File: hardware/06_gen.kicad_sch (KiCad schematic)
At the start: 0 parts

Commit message: Generator sheet: R-2R ladder and output stage
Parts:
- added C19: 470pF C0G, symbol Device:C
- added C20: 1nF C0G, symbol Device:C
- added C21: 100nF, symbol Device:C
- added J11: BNC_GEN, symbol Connector:Conn_Coaxial
- added J12: LINK2, Package_LCC:PLCC-44_16.6x16.6mm_P1.27mm, symbol Connector_Generic:Conn_01x02
- added R22, R23, R25, R27, R29, R31, R33, R35, R37: 20k, symbol Device:R
- added R24, R26, R28, R30, R32, R34, R36, R38: 10k, symbol Device:R
- added R39: 51R, symbol Device:R
- added U10: MCP6292, Package_TO_SOT_SMD:SOT-353_SC-70-5, symbol Amplifier_Operational:Opamp_Dual
- added U9: ESP32-S3-N16R8-DEVBOARD, RF_Module:ESP32-C3-WROOM-02, symbol oscil:ESP32-S3-N16R8-DEVBOARD
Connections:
- new net: R32.1, R33.2, R34.2
- new net: R30.1, R31.2, R32.2
- new net: R22.1, R23.2, R24.2
- new net: R26.1, R27.2, R28.2
- new net: C20.2, R39.1, U10.1, U10.2 (-)
- new net: J11.1 (In), R39.2
- new net: R24.1, R25.2, R26.2
- new net: C20.1, R36.1, R37.2, R38.2
- new net: R34.1, R35.2, R36.2
- new net: R28.1, R29.2, R30.2
- new net: C19.1, R38.1, U10.3 (+)
- new net: U10.6 (-), U10.7
- new net +3V3_GEN: C21.1, U10.8 (V+), U9.1 (3V3)
- new net +5V: U9.21 (5V)
- new net DAC_D0: R23.1, U9.4 (IO4)
- new net DAC_D1: R25.1, U9.5 (IO5)
- new net DAC_D2: R27.1, U9.6 (IO6)
- new net DAC_D3: R29.1, U9.7 (IO7)
- new net DAC_D4: R31.1, U9.12 (IO8)
- new net DAC_D5: R33.1, U9.15 (IO9)
- new net DAC_D6: R35.1, U9.16 (IO10)
- new net DAC_D7: R37.1, U9.17 (IO11)
- new net GND: C19.2, C21.2, J11.2 (Ext), J12.2 (Pin_2), R22.2, U10.4 (V-), U10.5 (+), U9.22 (GND), U9.23 (GND), U9.24 (GND), U9.44 (GND)
- new net LINK2_RX: J12.1 (Pin_1), U9.42 (IO44_RX)
- no-connect marks 0 -> 29
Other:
- note added: "2-pole Sallen-Key, unity gain. Ladder output is 10k, R38 10k. fc ~23kHz, Q ~0.73. C0G required."
- note added: "IO48: onboard WS2812 status LED, driven over RMT."
- note added: "Output 0 to 3.3V unipolar, no gain/offset stage in Rev A. 51R isolates the op-amp from cable capacitance."

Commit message: Add final Rev A schematic PDF and edited footprints
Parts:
- C19, C20, C21: footprint (none) -> Capacitor_THT:C_Disc_D5.0mm_W2.5mm_P5.00mm
- J11: footprint (none) -> Connector_Coaxial:BNC_PanelMountable_Vertical
- J12: footprint Package_LCC:PLCC-44_16.6x16.6mm_P1.27mm -> Connector_PinHeader_2.54mm:PinHeader_1x02_P2.54mm_Vertical
- R22, R23, R24, R25, R26, R27, R28, R29, R30, R31, R32, R33, R34, R35, R36, R37, R38, R39: footprint (none) -> Resistor_THT:R_Axial_DIN0207_L6.3mm_D2.5mm_P10.16mm_Horizontal
- U10: footprint Package_TO_SOT_SMD:SOT-353_SC-70-5 -> Package_DIP:DIP-8_W7.62mm
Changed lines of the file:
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@@
 	(title_block
 		(title "Oscil")
-		(date "2026-09-18")
-		(rev "0.1")
+		(date "2026-09-21")
+		(rev "A")
 		(comment 1 "Two-channel Digital Oscilloscope and Function Generator")
 		(comment 2 "ESP32-S3 / ESP-IDF / FreeRTOS")
@@
 			)
 		)
-		(property "Footprint" ""
+		(property "Footprint" "Resistor_THT:R_Axial_DIN0207_L6.3mm_D2.5mm_P10.16mm_Horizontal"
 			(at 121.92 135.382 90)
 			(hide yes)
@@
 			)
 		)
-		(property "Footprint" ""
+		(property "Footprint" "Resistor_THT:R_Axial_DIN0207_L6.3mm_D2.5mm_P10.16mm_Horizontal"
 			(at 109.982 129.54 90)
 			(hide yes)
@@
 			)
 		)
-		(property "Footprint" ""
+		(property "Footprint" "Resistor_THT:R_Axial_DIN0207_L6.3mm_D2.5mm_P10.16mm_Horizontal"
 			(at 28.702 129.54 90)
 			(hide yes)
@@
 			)
 		)
-		(property "Footprint" "Package_LCC:PLCC-44_16.6x16.6mm_P1.27mm"
+		(property "Footprint" "Connector_PinHeader_2.54mm:PinHeader_1x02_P2.54mm_Vertical"
 			(at 166.37 90.17 0)
 			(hide yes)
@@
 			)
 		)
-		(property "Footprint" ""
+		(property "Footprint" "Resistor_THT:R_Axial_DIN0207_L6.3mm_D2.5mm_P10.16mm_Horizontal"
 			(at 69.342 129.54 90)
 			(hide yes)
@@
 			)
 		)
-		(property "Footprint" ""
+		(property "Footprint" "Resistor_THT:R_Axial_DIN0207_L6.3mm_D2.5mm_P10.16mm_Horizontal"
 			(at 236.22 141.478 90)
 			(hide yes)
@@
 			)
 		)
-		(property "Footprint" ""
+		(property "Footprint" "Resistor_THT:R_Axial_DIN0207_L6.3mm_D2.5mm_P10.16mm_Horizontal"
 			(at 40.64 135.382 90)
 			(hide yes)
@@
 			)
 		)
-		(property "Footprint" "Package_TO_SOT_SMD:SOT-353_SC-70-5"
+		(property "Footprint" "Package_DIP:DIP-8_W7.62mm"
 			(at 228.6 95.25 0)
 			(hide yes)
@@
 			)
 		)
-		(property "Footprint" ""
+		(property "Footprint" "Capacitor_THT:C_Disc_D5.0mm_W2.5mm_P5.00mm"
 			(at 239.7252 97.79 0)
 			(hide yes)
@@
 			)
 		)
-		(property "Footprint" ""
+		(property "Footprint" "Connector_Coaxial:BNC_PanelMountable_Vertical"
 			(at 247.65 139.7 0)
 			(hide yes)
@@
 			)
 		)
-		(property "Footprint" ""
+		(property "Footprint" "Resistor_THT:R_Axial_DIN0207_L6.3mm_D2.5mm_P10.16mm_Horizontal"
 			(at 162.56 135.382 90)
 			(hide yes)
@@
 			)
 		)
-		(property "Footprint" ""
+		(property "Footprint" "Resistor_THT:R_Axial_DIN0207_L6.3mm_D2.5mm_P10.16mm_Horizontal"
 			(at 49.022 129.54 90)
 			(hide yes)
@@
 			)
 		)
-		(property "Footprint" ""
+		(property "Footprint" "Resistor_THT:R_Axial_DIN0207_L6.3mm_D2.5mm_P10.16mm_Horizontal"
 			(at 89.662 129.54 90)
 			(hide yes)
@@
 			)
 		)
-		(property "Footprint" ""
+		(property "Footprint" "Resistor_THT:R_Axial_DIN0207_L6.3mm_D2.5mm_P10.16mm_Horizontal"
 			(at 170.942 129.54 90)
 			(hide yes)
@@
 			)
 		)
-		(property "Footprint" ""
+		(property "Footprint" "Capacitor_THT:C_Disc_D5.0mm_W2.5mm_P5.00mm"
 			(at 191.77 123.4948 0)
 			(hide yes)
@@
 			)
 		)
-		(property "Footprint" ""
+		(property "Footprint" "Resistor_THT:R_Axial_DIN0207_L6.3mm_D2.5mm_P10.16mm_Horizontal"
 			(at 130.302 129.54 90)
 			(hide yes)
@@
 			)
 		)
-		(property "Footprint" ""
+		(property "Footprint" "Resistor_THT:R_Axial_DIN0207_L6.3mm_D2.5mm_P10.16mm_Horizontal"
 			(at 28.702 143.51 90)
 			(hide yes)
@@
 			)
 		)
-		(property "Footprint" ""
+		(property "Footprint" "Resistor_THT:R_Axial_DIN0207_L6.3mm_D2.5mm_P10.16mm_Horizontal"
 			(at 101.6 135.382 90)
 			(hide yes)
@@
 			)
 		)
-		(property "Footprint" ""
+		(property "Footprint" "Capacitor_THT:C_Disc_D5.0mm_W2.5mm_P5.00mm"
 			(at 196.5452 146.05 0)
 			(hide yes)
@@
 			)
 		)
-		(property "Footprint" ""
+		(property "Footprint" "Resistor_THT:R_Axial_DIN0207_L6.3mm_D2.5mm_P10.16mm_Horizontal"
 			(at 60.96 135.382 90)
 			(hide yes)
@@
 			)
 		)
-		(property "Footprint" "Package_TO_SOT_SMD:SOT-353_SC-70-5"
+		(property "Footprint" "Package_DIP:DIP-8_W7.62mm"
 			(at 220.98 139.7 0)
 			(hide yes)
@@
 			)
 		)
-		(property "Footprint" ""
+		(property "Footprint" "Resistor_THT:R_Axial_DIN0207_L6.3mm_D2.5mm_P10.16mm_Horizontal"
 			(at 142.24 135.382 90)
 			(hide yes)
@@
 			)
 		)
-		(property "Footprint" ""
+		(property "Footprint" "Resistor_THT:R_Axial_DIN0207_L6.3mm_D2.5mm_P10.16mm_Horizontal"
 			(at 81.28 135.382 90)
 			(hide yes)
@@
 			)
 		)
-		(property "Footprint" "Package_TO_SOT_SMD:SOT-353_SC-70-5"
+		(property "Footprint" "Package_DIP:DIP-8_W7.62mm"
 			(at 195.58 92.71 0)
 			(hide yes)
@@
 			)
 		)
-		(property "Footprint" ""
+		(property "Footprint" "Resistor_THT:R_Axial_DIN0207_L6.3mm_D2.5mm_P10.16mm_Horizontal"
 			(at 150.622 129.54 90)
 			(hide yes)
@@
 			)
 		)
-		(property "Footprint" ""
+		(property "Footprint" "Resistor_THT:R_Axial_DIN0207_L6.3mm_D2.5mm_P10.16mm_Horizontal"
 			(at 187.96 135.382 90)
 			(hide yes)

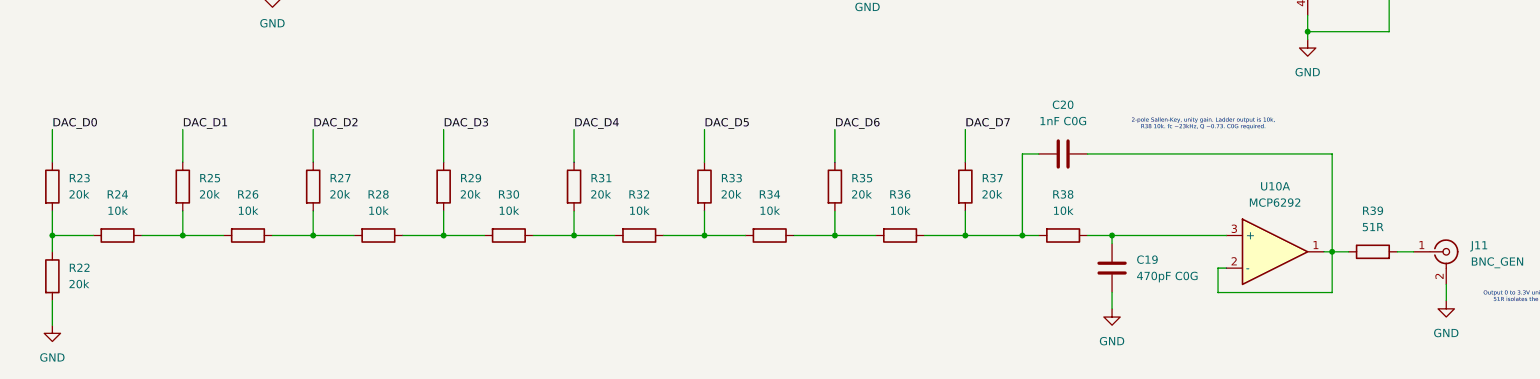
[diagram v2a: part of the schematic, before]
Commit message: hardware: generator ladder all 10k, R as parallel pairs, filter corner now 33 kHz; schematic exports regenerated
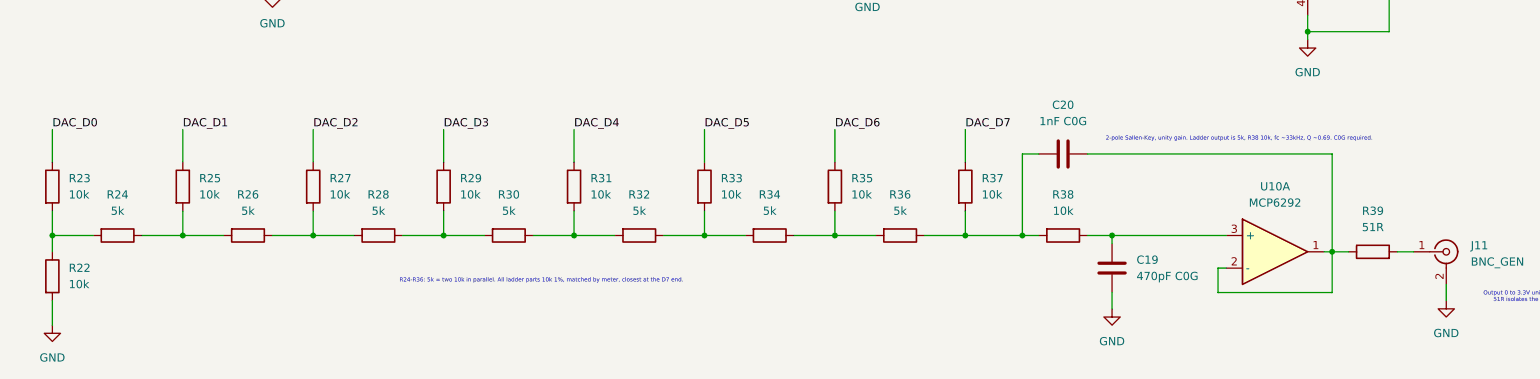
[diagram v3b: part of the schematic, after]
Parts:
- R22, R23, R25, R27, R29, R31, R33, R35, R37: value 20k -> 10k
- R24, R26, R28, R30, R32, R34, R36: value 10k -> 5k
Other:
- note added: "2-pole Sallen-Key, unity gain. Ladder output is 5k, R38 10k, fc ~33kHz, Q ~0.69. C0G required."
- note added: "R24-R36: 5k = two 10k in parallel. All ladder parts 10k 1%, matched by meter, closest at the D7 end."
- note removed: "2-pole Sallen-Key, unity gain. Ladder output is 10k, R38 10k. fc ~23kHz, Q ~0.73. C0G required."
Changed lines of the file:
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@@
 		(comment 2 "ESP32-S3 / ESP-IDF / FreeRTOS")
 	)
-	(text "2-pole Sallen-Key, unity gain. Ladder output is 10k,\nR38 10k. fc ~23kHz, Q ~0.73. C0G required."
+	(text "2-pole Sallen-Key, unity gain. Ladder output is 5k, R38 10k, fc ~33kHz, Q ~0.69. C0G required."
 		(exclude_from_sim no)
-		(at 209.804 119.888 0)
+		(at 215.392 122.174 0)
+		(effects
+			(font
+				(size 0.635 0.635)
+			)
+		)
+	)
+	(text "R24-R36: 5k = two 10k in parallel. All ladder parts 10k 1%, matched by meter, closest at the D7 end."
+		(exclude_from_sim no)
+		(at 106.68 144.272 0)
 		(effects
 			(font
@@
 			)
 		)
-		(property "Value" "10k"
+		(property "Value" "5k"
 			(at 121.92 133.35 90)
 			(show_name no)
@@
 			)
 		)
-		(property "Value" "20k"
+		(property "Value" "10k"
 			(at 114.3 130.8099 0)
 			(show_name no)
@@
 			)
 		)
-		(property "Value" "20k"
+		(property "Value" "10k"
 			(at 33.02 130.8099 0)
 			(show_name no)
@@
 			)
 		)
-		(property "Value" "20k"
+		(property "Value" "10k"
 			(at 73.66 130.8099 0)
 			(show_name no)
@@
 			)
 		)
-		(property "Value" "10k"
+		(property "Value" "5k"
 			(at 40.64 133.35 90)
 			(show_name no)
@@
 			)
 		)
-		(property "Value" "10k"
+		(property "Value" "5k"
 			(at 162.56 133.35 90)
 			(show_name no)
@@
 			)
 		)
-		(property "Value" "20k"
+		(property "Value" "10k"
 			(at 53.34 130.8099 0)
 			(show_name no)
@@
 			)
 		)
-		(property "Value" "20k"
+		(property "Value" "10k"
 			(at 93.98 130.8099 0)
 			(show_name no)
@@
 			)
 		)
-		(property "Value" "20k"
+		(property "Value" "10k"
 			(at 175.26 130.8099 0)
 			(show_name no)
@@
 			)
 		)
-		(property "Value" "20k"
+		(property "Value" "10k"
 			(at 134.62 130.8099 0)
 			(show_name no)
@@
 			)
 		)
-		(property "Value" "20k"
+		(property "Value" "10k"
 			(at 33.02 144.7799 0)
 			(show_name no)
@@
 			)
 		)
-		(property "Value" "10k"
+		(property "Value" "5k"
 			(at 101.6 133.35 90)
 			(show_name no)
@@
 			)
 		)
-		(property "Value" "10k"
+		(property "Value" "5k"
 			(at 60.96 133.35 90)
 			(show_name no)
@@
 			)
 		)
-		(property "Value" "10k"
+		(property "Value" "5k"
 			(at 142.24 133.35 90)
 			(show_name no)
@@
 			)
 		)
-		(property "Value" "10k"
+		(property "Value" "5k"
 			(at 81.28 133.35 90)
 			(show_name no)
@@
 			)
 		)
-		(property "Value" "20k"
+		(property "Value" "10k"
 			(at 154.94 130.8099 0)
 			(show_name no)
